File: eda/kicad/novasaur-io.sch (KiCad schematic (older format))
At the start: 73 parts, among them J1 POWER IN, J3 AUDIO OUT, J4 KEYBOARD, J5 SERIAL, J5 SPKR, J6 DISPLAY, J7 EXPANSION, J8 EXP OUT, J9 VIDEO, Q1 2N3904, Q2 2N3904, Q4 BS270, SW1 POWER, U1 74F86, U2 74F08, U38 CD4053, U39 MAX232, U4 74F32, U40 NJM4580, U41 MCP1827S, U6 74F139, U7 74F139

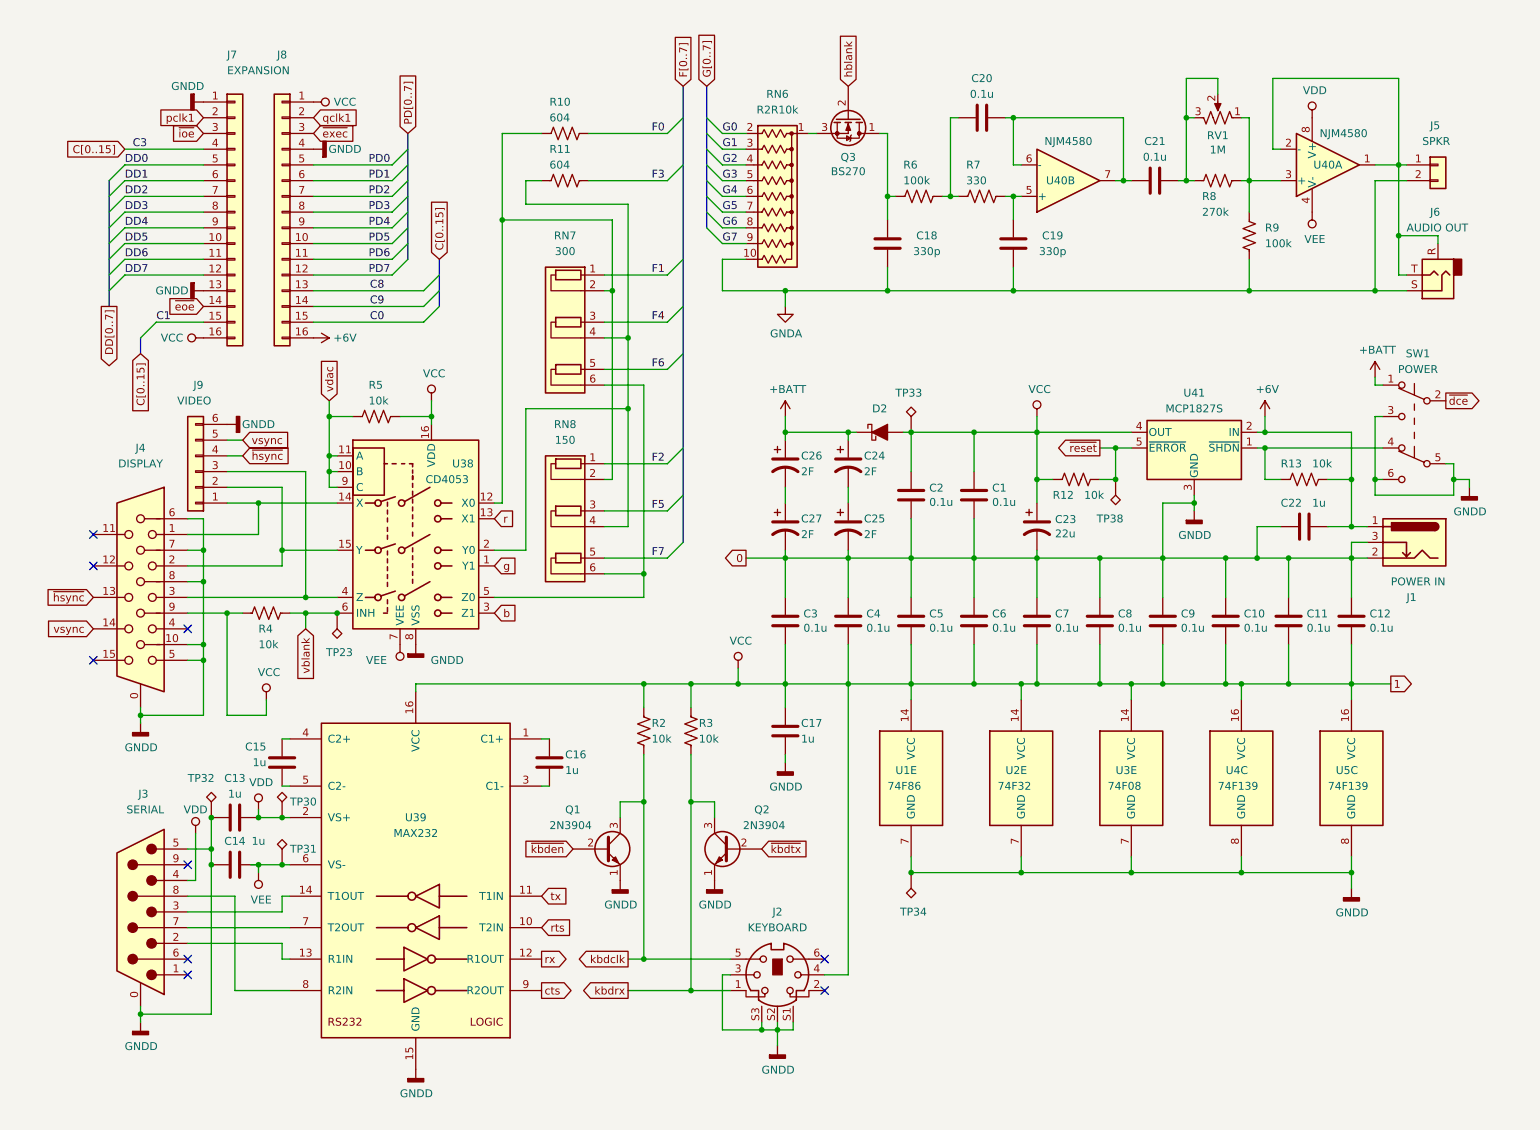
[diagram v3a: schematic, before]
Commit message: Fix audio Updates to make audio work after testing
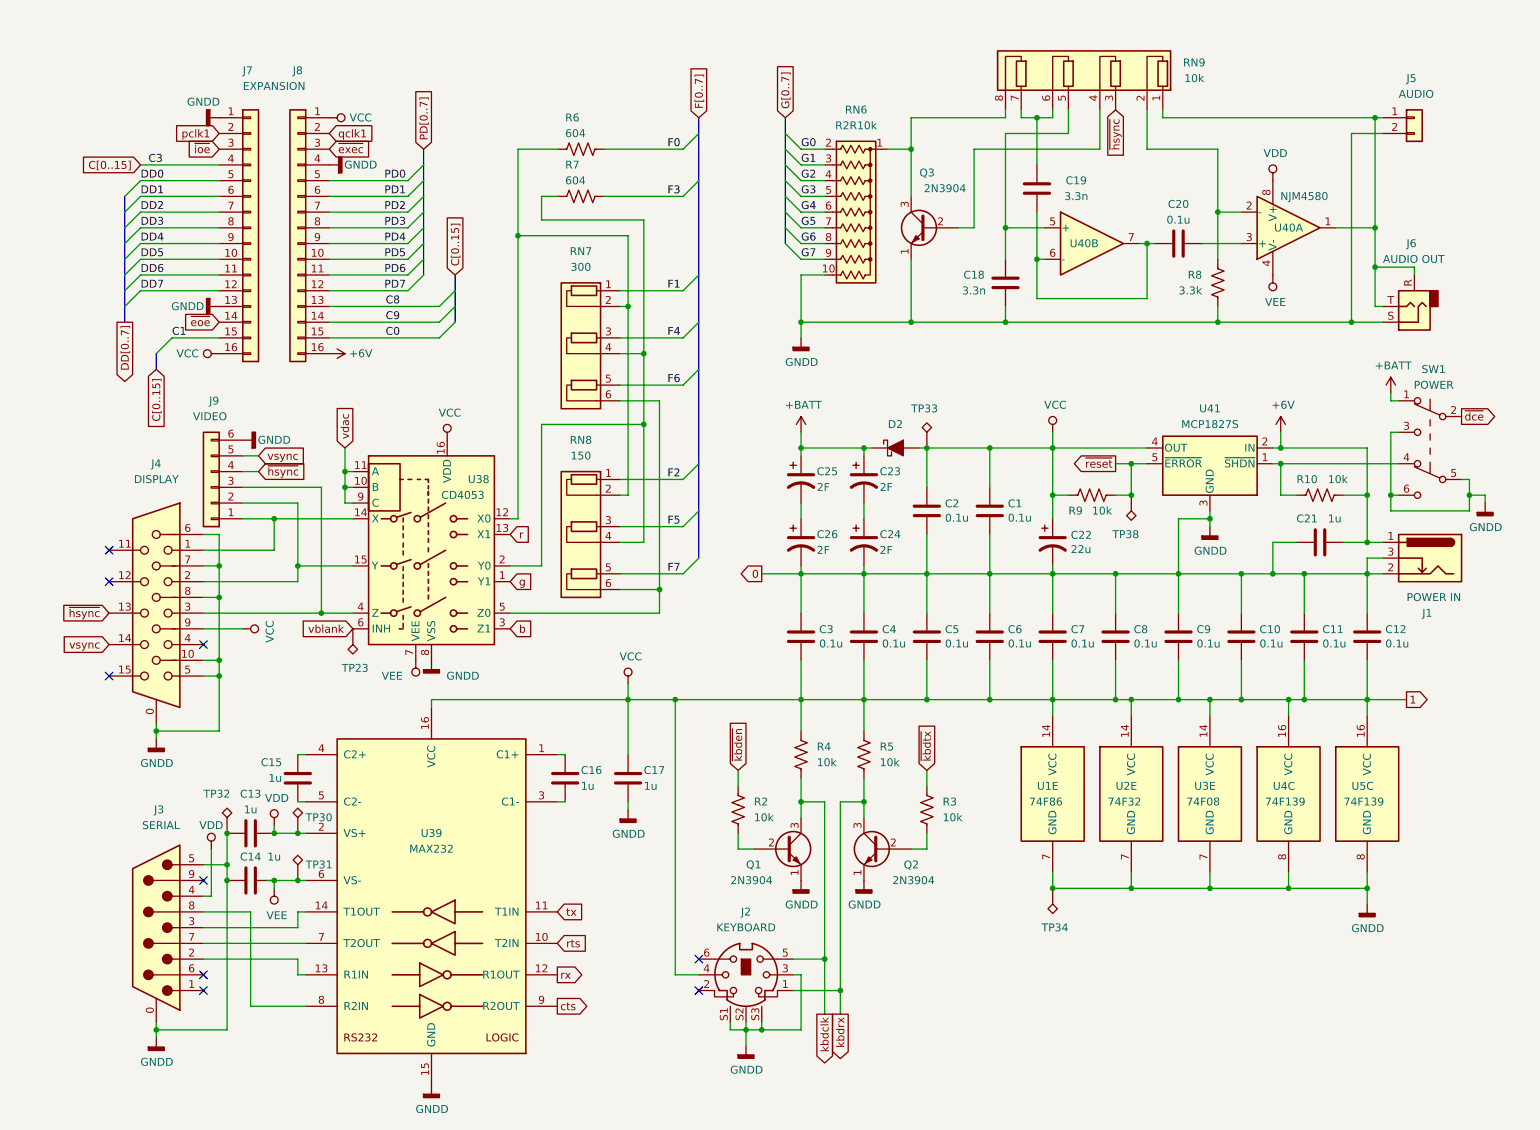
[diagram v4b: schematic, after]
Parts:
- removed C18: 330p, Capacitor_THT:C_Disc_D3.0mm_W2.0mm_P2.50mm, symbol Device:C
- removed C20: 0.1u, Capacitor_THT:C_Disc_D5.0mm_W2.5mm_P5.00mm, symbol Device:C
- removed Q4: BS270, Package_TO_SOT_THT:TO-92_HandSolder, symbol Transistor_FET:BS170
- removed R5 (x2): 10k, Resistor_THT:R_Axial_DIN0204_L3.6mm_D1.6mm_P7.62mm_Horizontal, symbol Device:R_US
- removed R6, R9: 100k, Resistor_THT:R_Axial_DIN0204_L3.6mm_D1.6mm_P7.62mm_Horizontal, symbol Device:R_US
- removed R7: 330, Resistor_THT:R_Axial_DIN0204_L3.6mm_D1.6mm_P7.62mm_Horizontal, symbol Device:R_US
- removed RV1: 1M, Potentiometer_THT:Potentiometer_Piher_PT-10-H01_Horizontal, symbol Device:R_POT_US
- added C19: 3.3n, Capacitor_THT:C_Disc_D3.0mm_W2.0mm_P2.50mm, symbol Device:C
- added Q3: 2N3904, Package_TO_SOT_THT:TO-92_HandSolder, symbol Transistor_BJT:2N3904
- added R2, R5: 10k, Resistor_THT:R_Axial_DIN0204_L3.6mm_D1.6mm_P7.62mm_Horizontal, symbol Device:R_US
- added RN9: 10k, Resistor_THT:R_Array_SIP8, symbol Device:R_Pack04_SIP
- C7: value 330p -> 3.3n
- J5: value SPKR -> AUDIO
- R8: value 270k -> 3.3k
- renumbered C22 to C21, C23 to C22, C24 to C23, C25 to C24, C26 to C25, C27 to C26, R13 to R10, R10 to R6, R11 to R7, R12 to R9
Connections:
- net GNDA is gone; now on net GNDD: C7.2, J3.S, J5.2 (Pin_2), RN6.10 (R9)
- net GNDD: now also R8.1, Q3.1 (E)
- net VCC: now also R4.1, R5.1; no longer R3.1, R4.2
- net kbdclk: now also R4.2
- net kbdrx: now also R5.2; no longer R3.2
- net vblank: no longer R4.1
- net ~hsync: now also RN9.3 (R2.1)
- net ~kbden: now also R2.1; no longer Q1.2 (B)
- net ~kbdtx: now also R3.1; no longer Q2.2 (B)
- net at U40.3 (+): now also C5.2; no longer R8.1
- net at R8.2: now also U40.2 (-), RN9.2 (R1.2); no longer C5.2
- net at C5.1, U40.6 (-), U40.7: now also C19.2
- net at C7.1, U40.5 (+): now also RN9.5 (R3.1)
- net at J3.R, J3.T, J5.1 (Pin_1)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: now also RN9.1 (R1.1); no longer U40.2 (-)
- net at RN6.1 (common): now also Q3.3 (C), RN9.8 (R4.2)
- new net: C19.1, RN9.6 (R3.2), RN9.7 (R4.1)
- new net: Q1.2 (B), R2.2
- new net: Q2.2 (B), R3.2
- new net: Q3.2 (B), RN9.4 (R2.2)
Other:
- moved on the sheet: C1, C10, C11, C12, C13, C14, C15, C16, C17, C18, C2, C20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

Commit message: audio muting and updated filter/inverting amplifier
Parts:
- added R8: 330, Resistor_THT:R_Axial_DIN0204_L3.6mm_D1.6mm_P7.62mm_Horizontal, symbol Device:R_US
- C19, C7: value 3.3n -> 330p
- C5: value 0.1u -> 1u
- R9: renamed from R8; value 3.3k -> 10k
- RN9: value 10k -> 100k; footprint Resistor_THT:R_Array_SIP8 -> Resistor_THT:R_Array_SIP6; symbol Device:R_Pack04_SIP -> Device:R_Pack03_SIP
- renumbered R9 to R10, R10 to R11
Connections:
- net GNDD: now also U40.3 (+); no longer R9.1
- net ~hsync: now also R8.2; no longer RN9.3 (R2.1)
- net ~kbdtx: now also R3.2; no longer R3.1
- net at Q3.3 (C), RN6.1 (common): now also RN9.3 (R2.1); no longer RN9.8 (R4.2)
- net at C19.2, C5.1, U40.7: now also U40.5 (+); no longer U40.6 (-)
- net at Q2.2 (B): now also R3.1; no longer R3.2
- net at RN9.4 (R2.2): now also C19.1, RN9.5 (R3.1); no longer Q3.2 (B)
- net at C5.2: now also R9.1; no longer U40.3 (+)
- new net: Q3.2 (B), R8.1
- new net: C7.1, RN9.6 (R3.2), U40.6 (-)
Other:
- moved on the sheet: C19, C20, J2, J5, Q1, Q2, Q3, R2, R3, R4, R5, R9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

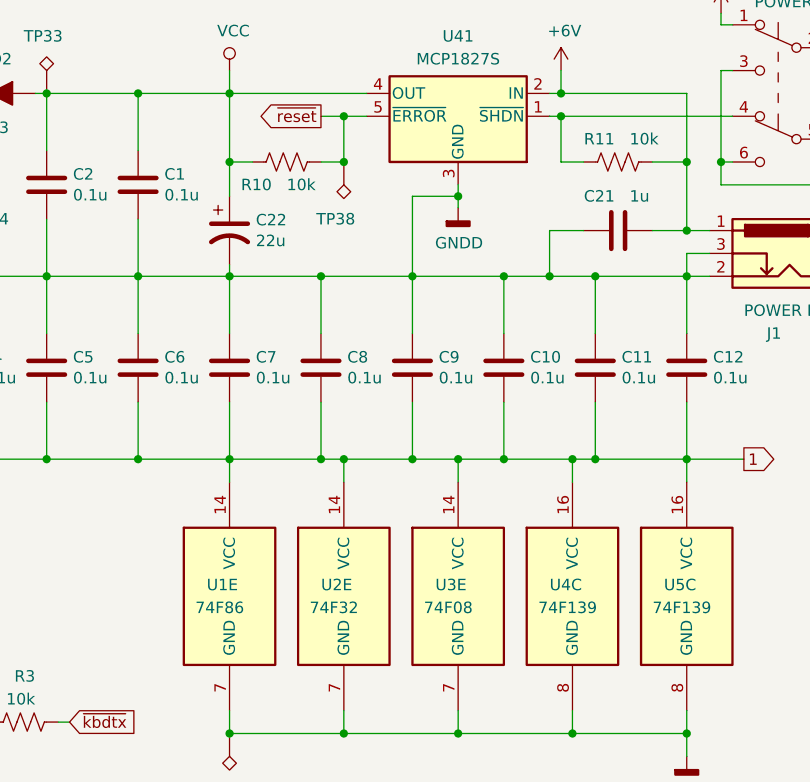
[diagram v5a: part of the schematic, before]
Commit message: rev 8 schematic stop FCP during blanking
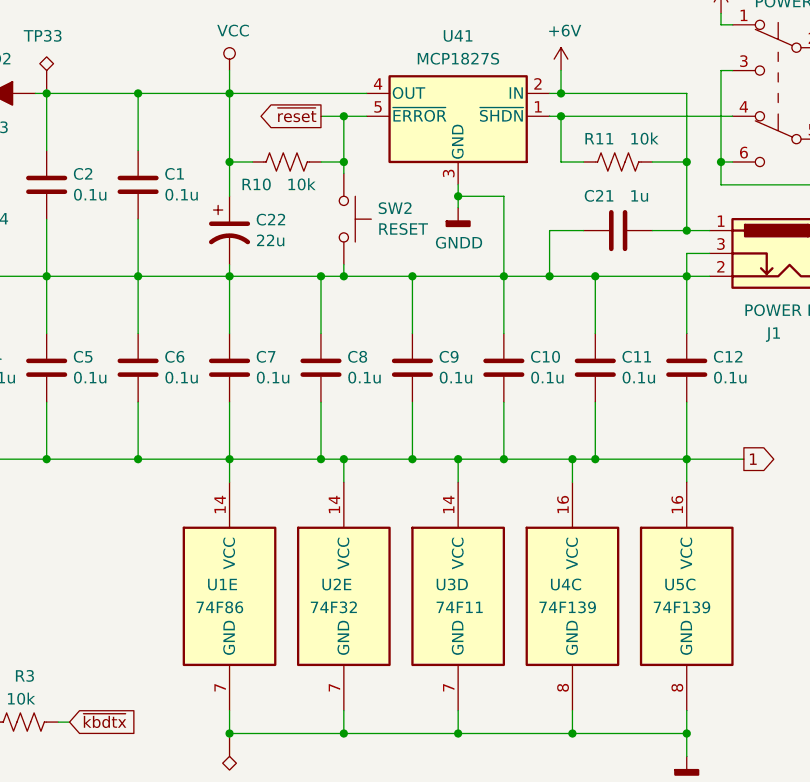
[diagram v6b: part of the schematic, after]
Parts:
- removed TP38: RESET, TestPoint:TestPoint_THTPad_1.0x1.0mm_Drill0.5mm, symbol Connector:TestPoint_Alt
- removed U2: 74F08, Package_DIP:DIP-14_W7.62mm_LongPads, symbol 74xx:74LS08
- added SW2: RESET, TestPoint:TestPoint_2Pads_Pitch2.54mm_Drill0.8mm, symbol Switch:SW_Push
- added U3: 74F11, Package_DIP:DIP-14_W7.62mm_LongPads, symbol 74xx:74LS11
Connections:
- net GNDD: now also SW2.2, U3.7 (GND)
- net VCC: now also U3.14 (VCC)
- net ~reset: now also SW2.1
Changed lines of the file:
@@
 Sheet 4 4
 Title "Input/Output"
-Date "2020-10-01"
-Rev "1.7"
+Date "2020-10-10"
+Rev "1.8"
 Comp ""
 Comment1 "(c) A J Hewitt 2020"
@@
 $EndComp
 $Comp
-L 74xx:74LS08 U?
-U 5 1 63199762
-P 8150 5600
-AR Path="/5CDEEC9F/63199762" Ref="U?"  Part="5"
-AR Path="/63199762" Ref="U?"  Part="5"
-AR Path="/62D13D9D/63199762" Ref="U2"  Part="5"
-AR Path="/5DAA5CD8/5D9AFF37/63199762" Ref="U?"  Part="5"
-AR Path="/5DA1E9C0/63199762" Ref="U3"  Part="5"
-F 0 "U3" H 8050 5650 50  0000 L CNN
-F 1 "74F08" H 8000 5550 50  0000 L CNN
-F 2 "Package_DIP:DIP-14_W7.62mm_LongPads" H 8150 5600 50  0001 C CNN
-F 3 "http://www.ti.com/lit/gpn/sn74LS08" H 8150 5600 50  0001 C CNN
-	5    8150 5600
-	1    0    0    -1
-$EndComp
-$Comp
 L 74xx:74LS32 U?
 U 5 1 63199778
@@
 	0    1    1    0
 $EndComp
-$Comp
-L Connector:TestPoint_Alt TP?
-U 1 1 5EF37DC4
-P 7650 3700
-AR Path="/5EF37DC4" Ref="TP?"  Part="1"
-AR Path="/5DA1E9BA/5EF37DC4" Ref="TP?"  Part="1"
-AR Path="/5DA1E9BD/5EF37DC4" Ref="TP?"  Part="1"
-AR Path="/5DA1E9C0/5EF37DC4" Ref="TP38"  Part="1"
-F 0 "TP38" H 7600 3950 50  0000 L CNN
-F 1 "RESET" H 7400 3850 50  0001 L CNN
-F 2 "TestPoint:TestPoint_THTPad_1.0x1.0mm_Drill0.5mm" H 7850 3700 50  0001 C CNN
-F 3 "~" H 7850 3700 50  0001 C CNN
-	1    7650 3700
-	-1   0    0    1
-$EndComp
-Connection ~ 7650 3700
 Wire Wire Line
 	8550 3500 8600 3500
@@
 	8550 4000 8550 4200
 Connection ~ 9150 4000
-Wire Wire Line
-	8150 3800 8150 3850
-Connection ~ 8150 3850
-Wire Wire Line
-	8150 3850 8150 3900
-Wire Wire Line
-	7950 4200 7950 3850
-Wire Wire Line
-	7950 3850 8150 3850
-Wire Wire Line
-	7550 4200 7950 4200
 Wire Wire Line
 	8600 3700 8700 3700
@@
 Wire Wire Line
 	6950 1350 6950 1400
-Wire Bus Line
-	3350 2300 3350 2600
-Wire Bus Line
-	3150 1500 3150 2300
-Wire Bus Line
-	1250 1800 1250 2600
-Wire Bus Line
-	5450 1300 5450 2100
-Wire Bus Line
-	4900 1300 4900 4100
 $Comp
 L Device:R_Pack03_SIP RN9
@@
 	-1   0    0    -1
 $EndComp
+Wire Wire Line
+	8150 3800 8150 3850
+Wire Wire Line
+	8350 4200 8350 3850
+Wire Wire Line
+	8350 3850 8150 3850
+Connection ~ 8150 3850
+Wire Wire Line
+	8150 3850 8150 3900
+$Comp
+L Switch:SW_Push SW2
+U 1 1 5F8FCEDE
+P 7650 3950
+F 0 "SW2" V 7604 4098 50  0000 L CNN
+F 1 "RESET" V 7695 4098 50  0000 L CNN
+F 2 "TestPoint:TestPoint_2Pads_Pitch2.54mm_Drill0.8mm" H 7650 4150 50  0001 C CNN
+F 3 "~" H 7650 4150 50  0001 C CNN
+	1    7650 3950
+	0    1    1    0
+$EndComp
+Wire Wire Line
+	7550 4200 7650 4200
+Wire Wire Line
+	7650 3750 7650 3700
+Connection ~ 7650 3700
+Wire Wire Line
+	7650 4150 7650 4200
+Connection ~ 7650 4200
+Wire Wire Line
+	7650 4200 7950 4200
+$Comp
+L 74xx:74LS11 U3
+U 4 1 5F956C3E
+P 8150 5600
+F 0 "U3" H 8050 5650 50  0000 L CNN
+F 1 "74F11" H 8050 5550 50  0000 L CNN
+F 2 "Package_DIP:DIP-14_W7.62mm_LongPads" H 8150 5600 50  0001 C CNN
+F 3 "http://www.ti.com/lit/gpn/sn74LS11" H 8150 5600 50  0001 C CNN
+	4    8150 5600
+	1    0    0    -1
+$EndComp
+Wire Bus Line
+	3350 2300 3350 2600
+Wire Bus Line
+	3150 1500 3150 2300
+Wire Bus Line
+	5450 1300 5450 2100
+Wire Bus Line
+	1250 1800 1250 2600
+Wire Bus Line
+	4900 1300 4900 4100
 $EndSCHEMATC
